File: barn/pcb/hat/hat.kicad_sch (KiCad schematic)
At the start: 17 parts, among them J1 Conn_01x02, J2 Conn_01x04, J3 Conn_02x13_Odd_Even, J4 Conn_01x02, Q1 BC547, Q2 BC547, SW1 SW_Push_DPDT, U1 buck-converter

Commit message: Finish routing.
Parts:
- removed Q1, Q2: BC547, Package_TO_SOT_THT:TO-92_HandSolder, symbol Device:Q_NPN_BCE
- added J5, J6: Conn_01x02, Connector_JST:JST_XH_B2B-XH-A_1x02_P2.50mm_Vertical, symbol Connector_Generic:Conn_01x02
- added Q1, Q2: BC547, Package_TO_SOT_THT:TO-92_HandSolder, symbol Device:Q_NPN_CBE
- C1, C2: value 100u -> 10u; footprint (none) -> Capacitor_THT:CP_Radial_D8.0mm_P5.00mm
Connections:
- net +12V: now also J5.1 (Pin_1)
- net +3V3: now also J2.1 (Pin_1), SW1.1 (A)
- net +5V: now also J6.1 (Pin_1)
- net GND: now also J2.2 (Pin_2), J5.2 (Pin_2), J6.2 (Pin_2), Q1.3 (E), Q2.3 (E)
- net SCL: now also J2.3 (Pin_3)
- net SDA: now also J2.4 (Pin_4)
- net at D1.2 (A), RL1.1: now also Q1.1 (C)
- net at D2.2 (A), RL2.1: now also Q2.1 (C)
- net GPIO22: now reaches J3.15 (Pin_15)
- net GPIO22: now also R3.1, SW1.2 (B), SW1.5 (B)
- net GPIO10: now reaches J3.19 (Pin_19)
- net GPIO10: now also R2.1
- net at R1.2: now also Q1.2 (B)
- net at R2.2: now also Q2.2 (B)
- removed net GPIO?: R2.1, R3.1, SW1.5 (B)
- no-connect marks 13 -> 15
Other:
- note added: "12V IN"

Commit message: Finish routing.
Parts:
- removed J3: Conn_02x13_Odd_Even, Connector_PinHeader_2.54mm:PinHeader_2x13_P2.54mm_Vertical, symbol Connector_Generic:Conn_02x13_Odd_Even
- removed U1: buck-converter, legacy:buck-converter, symbol buck-converter:buck-converter
- added C3: 100u/16V, Capacitor_Tantalum_SMD:CP_EIA-7343-43_Kemet-X, symbol Device:C_Polarized
- added J6: Conn_02x13_Odd_Even, Connector_PinSocket_2.54mm:PinSocket_2x13_P2.54mm_Vertical, symbol Connector_Generic:Conn_02x13_Odd_Even
- added J7: Conn_01x13, Connector_PinSocket_2.54mm:PinSocket_1x13_P2.54mm_Vertical, symbol Connector_Generic:Conn_01x13
- added L1: 10m, Inductor_THT:L_Radial_D8.7mm_P5.00mm_Fastron_07HCP, symbol Device:L_Ferrite
- C1, C2: footprint Capacitor_THT:CP_Radial_D8.0mm_P5.00mm -> Capacitor_Tantalum_SMD:CP_EIA-6032-28_Kemet-C
- D1, D2: footprint Diode_THT:D_A-405_P7.62mm_Horizontal -> Diode_SMD:D_MiniMELF
- J5: renamed from J2; footprint Connector_PinHeader_2.54mm:PinHeader_1x04_P2.54mm_Vertical -> Connector_PinSocket_2.54mm:PinSocket_1x04_P2.54mm_Vertical
- Q1, Q2: value BC547 -> MMBT3904; footprint Package_TO_SOT_THT:TO-92_HandSolder -> Package_TO_SOT_SMD:SOT-23; symbol Device:Q_NPN_CBE -> Device:Q_NPN_BEC
- R1, R2, R3: footprint Resistor_THT:R_Axial_DIN0207_L6.3mm_D2.5mm_P10.16mm_Horizontal -> Resistor_SMD:R_0603_1608Metric
- renumbered J5 to J1, J6 to J2, J1 to J3
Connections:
- net +3V3: now also J6.1 (Pin_1)
- net +5V: now also C3.1, J6.2 (Pin_2), J6.4 (Pin_4), L1.2; no longer J2.1 (Pin_1)
- net GND: now also Q1.2 (E), Q2.2 (E), C3.2, J6.14 (Pin_14), J6.20 (Pin_20), J6.25 (Pin_25), J6.6 (Pin_6), J6.9 (Pin_9); no longer Q1.3 (E), Q2.3 (E)
- net SCL: now also J6.5 (Pin_5)
- net SDA: now also J6.3 (Pin_3)
- net at D1.2 (A), RL1.1: now also Q1.3 (C); no longer Q1.1 (C)
- net at D2.2 (A), RL2.1: now also Q2.3 (C); no longer Q2.1 (C)
- net at R1.2: now also Q1.1 (B); no longer Q1.2 (B)
- net at R2.2: now also Q2.1 (B); no longer Q2.2 (B)
- net GPIO10 renamed GPIO0
- net GPIO0: now also J6.13 (Pin_13)
- net GPIO22 renamed GPIO6
- net GPIO6: now also J6.7 (Pin_7)
- net GPIO4 renamed GPIO1
- net GPIO1: now also J6.11 (Pin_11)
- new net: J2.1 (Pin_1), L1.1
- no-connect marks 15 -> 28

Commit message: Fill zones.
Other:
- note added: "5V IN"
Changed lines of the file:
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@@
+    (effects (font (size 1.27 1.27)) (justify left bottom))
+  )
+  (text "5V IN" (at 200.66 92.964 0)
     (effects (font (size 1.27 1.27)) (justify left bottom))
   )

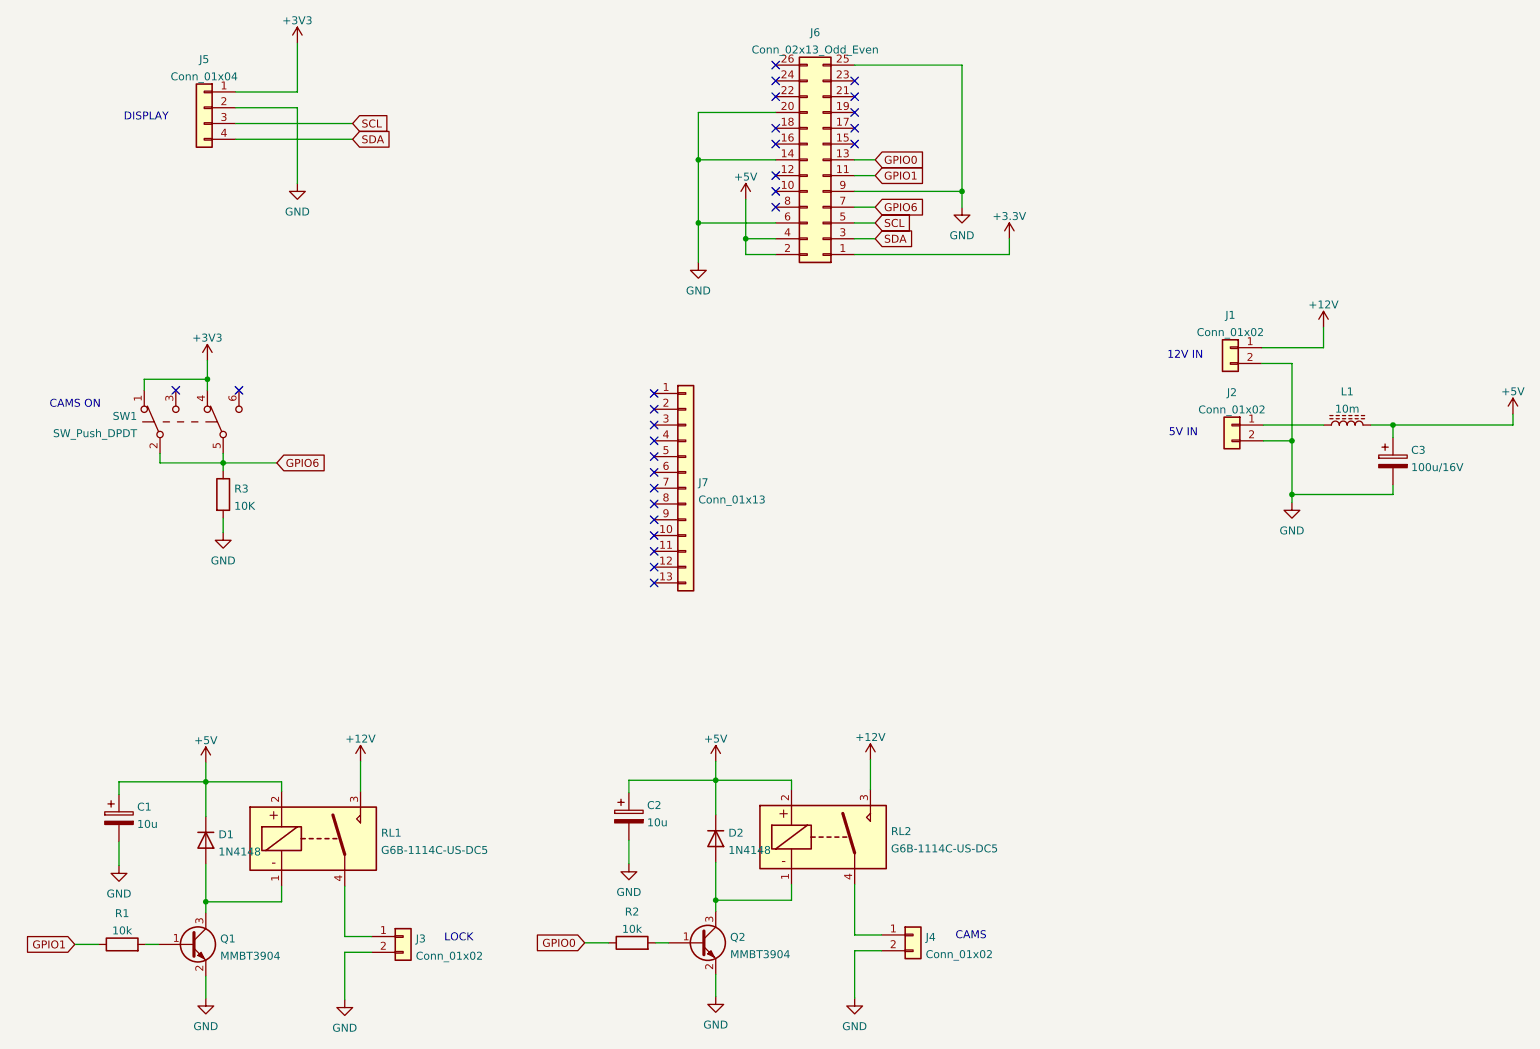
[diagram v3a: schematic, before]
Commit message: Add input for door switch.
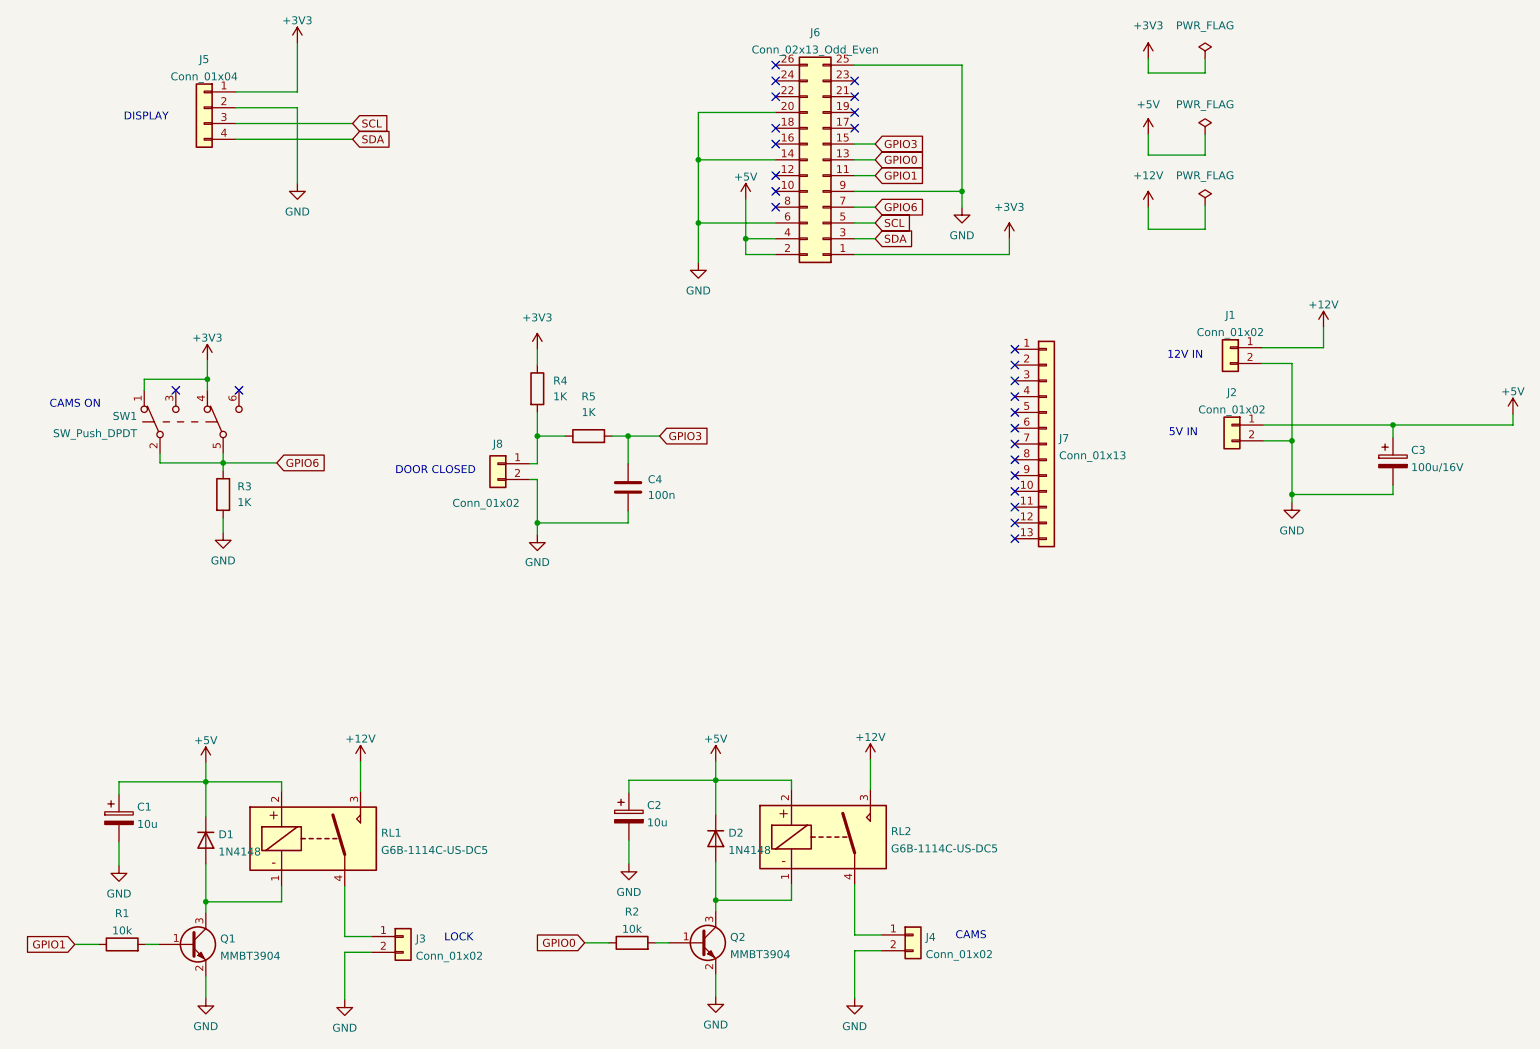
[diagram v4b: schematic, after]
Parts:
- removed L1: 10m, Inductor_THT:L_Radial_D8.7mm_P5.00mm_Fastron_07HCP, symbol Device:L_Ferrite
- added C4: 100n, Capacitor_SMD:C_0603_1608Metric, symbol Device:C
- added J8: Conn_01x02, Connector_JST:JST_XH_B2B-XH-A_1x02_P2.50mm_Vertical, symbol Connector_Generic:Conn_01x02
- added R4, R5: 1K, Resistor_SMD:R_0603_1608Metric, symbol Device:R
- R3: value 10K -> 1K
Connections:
- net +3V3: now also R4.1
- net +5V: now also J2.1 (Pin_1)
- net GND: now also C4.2, J8.2 (Pin_2)
- net GPIO3: now reaches J6.15 (Pin_15)
- net GPIO3: now also C4.1, R5.2
- new net: J8.1 (Pin_1), R4.2, R5.1
- no-connect marks 28 -> 27
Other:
- note added: "DOOR CLOSED"
- moved on the sheet: J7
